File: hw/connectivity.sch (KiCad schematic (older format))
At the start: 130 parts, among them P1 CONN_13X3, P10 MICROSD, P11 CONN_9, P12 CONN_2, P13 CONN_6, P19 CONN_1, P2 CONN_4, P20 CONN_1, P21 CONN_1, P22 CONN_1, P3 CONN_4, P4 MICROUSB, P5 CONN_4, P6 CONN_6, P7 CONN_4, P8 CONN_4, P9 CONN_4, Q2 NTA4153NT1G, Q3 NTA4151PT1G, Q4 PDTC114EE, Q5 PDTC114EE, Q6 PDTC114EE, Q7 PDTC114EE, SW1 STG719, U1 XBEE, U11 SN74AHC1G86, U12 MAX4090, U2 LTC4411, U3 SN65HVD233, U4 ADP3338AKCZ-3.3, U5 LT1761-3.3, U6 EL1883

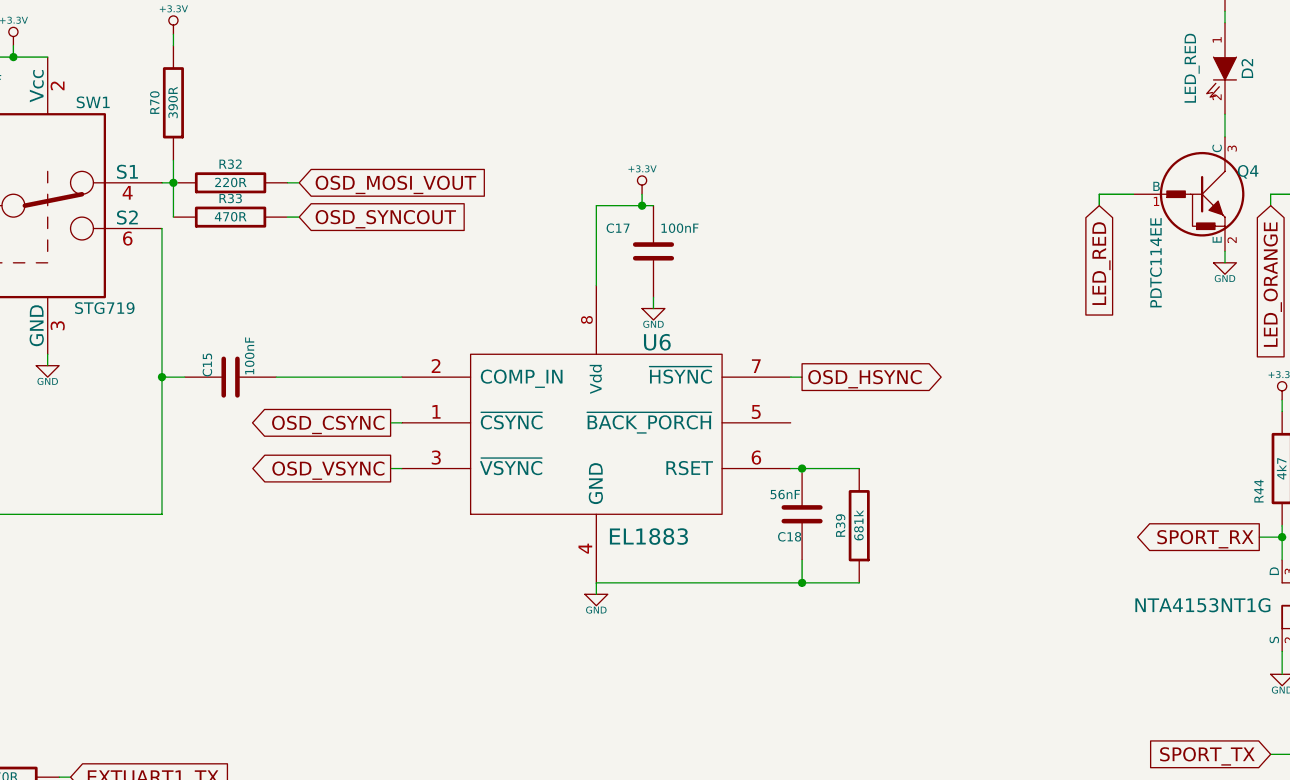
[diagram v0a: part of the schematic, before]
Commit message: hw: add chroma filter to sync separator, removed unused CSYNC signal
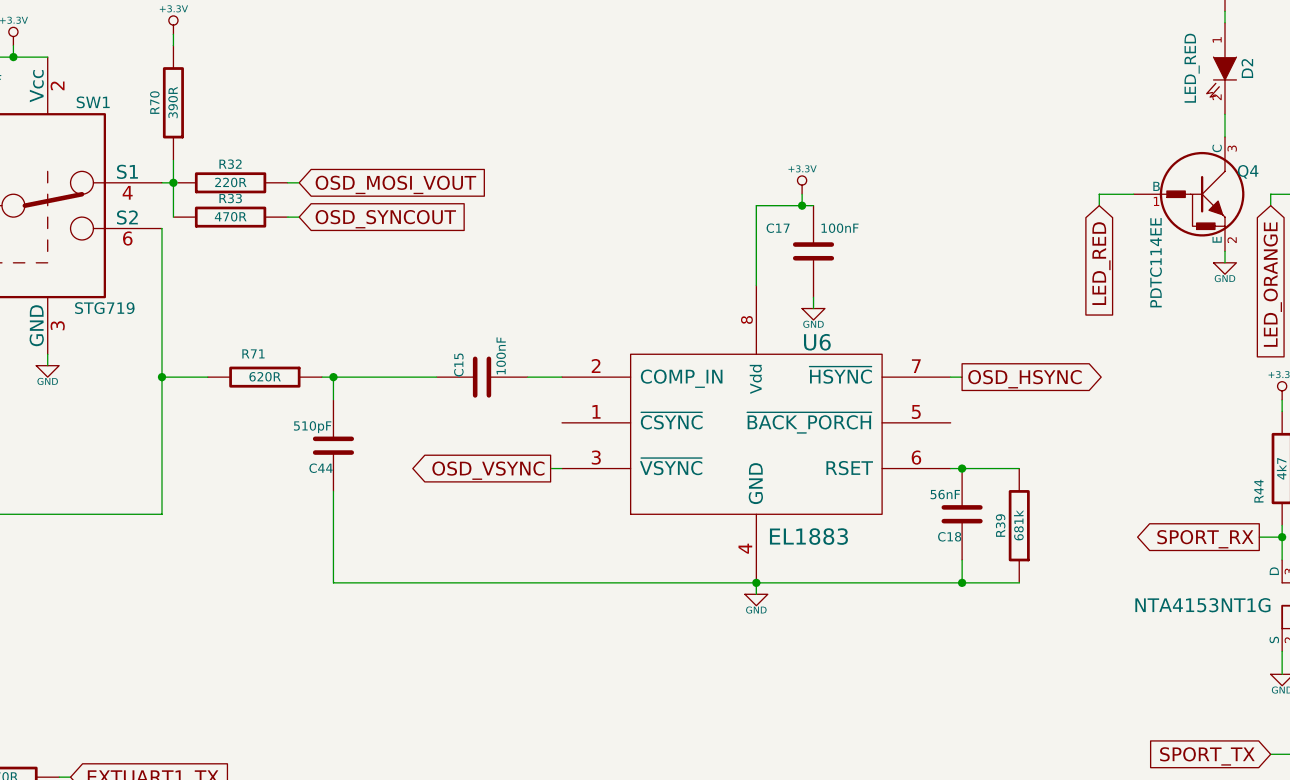
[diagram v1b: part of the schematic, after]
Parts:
- added C44: 510pF, c_0603, symbol C
- added R71: 620R, r_0603, symbol R
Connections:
- net labels removed: OSD_CSYNC
- wire segments 325 -> 327
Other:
- moved on the sheet: C15, C17, C18, R39, U6
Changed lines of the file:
@@
 L EL1883 U6
 U 1 1 52531AD1
-P 10800 5350
-F 0 "U6" H 11000 5750 70  0000 L CNN
-F 1 "EL1883" H 10850 4900 70  0000 L CNN
-F 2 "so-8" H 10800 5350 60  0001 C CNN
-F 3 "~" H 10800 5350 60  0000 C CNN
-	1    10800 5350
+P 11500 5350
+F 0 "U6" H 11700 5750 70  0000 L CNN
+F 1 "EL1883" H 11550 4900 70  0000 L CNN
+F 2 "so-8" H 11500 5350 60  0001 C CNN
+F 3 "~" H 11500 5350 60  0000 C CNN
+	1    11500 5350
 	1    0    0    -1
 $EndComp
@@
 L C C15
 U 1 1 525457CD
-P 9200 5100
-F 0 "C15" H 9200 5200 40  0000 L CNN
-F 1 "100nF" H 9206 5015 40  0000 L CNN
-F 2 "c_0603" H 9238 4950 30  0001 C CNN
-F 3 "~" H 9200 5100 60  0000 C CNN
-	1    9200 5100
-	0    -1   -1   0
-$EndComp
-Wire Wire Line
-	8900 5100 9000 5100
-Wire Wire Line
-	9400 5100 9950 5100
+P 10300 5100
+F 0 "C15" H 10300 5200 40  0000 L CNN
+F 1 "100nF" H 10306 5015 40  0000 L CNN
+F 2 "c_0603" H 10338 4950 30  0001 C CNN
+F 3 "~" H 10300 5100 60  0000 C CNN
+	1    10300 5100
+	0    -1   -1   0
+$EndComp
+Wire Wire Line
+	8900 5100 9100 5100
 $Comp
 L C C18
 U 1 1 52545C9B
-P 11700 5700
-F 0 "C18" H 11700 5800 40  0000 L CNN
-F 1 "56nF" H 11706 5615 40  0000 L CNN
-F 2 "c_0603" H 11738 5550 30  0001 C CNN
-F 3 "~" H 11700 5700 60  0000 C CNN
-	1    11700 5700
+P 12400 5700
+F 0 "C18" H 12400 5800 40  0000 L CNN
+F 1 "56nF" H 12406 5615 40  0000 L CNN
+F 2 "c_0603" H 12438 5550 30  0001 C CNN
+F 3 "~" H 12400 5700 60  0000 C CNN
+	1    12400 5700
 	-1   0    0    1
 $EndComp
@@
 L R R39
 U 1 1 52545CAD
-P 11950 5750
-F 0 "R39" V 12030 5750 40  0000 C CNN
-F 1 "681k" V 11950 5750 40  0000 C CNN
-F 2 "r_0603" V 11880 5750 30  0001 C CNN
-F 3 "~" H 11950 5750 30  0000 C CNN
-	1    11950 5750
+P 12650 5750
+F 0 "R39" V 12730 5750 40  0000 C CNN
+F 1 "681k" V 12650 5750 40  0000 C CNN
+F 2 "r_0603" V 12580 5750 30  0001 C CNN
+F 3 "~" H 12650 5750 30  0000 C CNN
+	1    12650 5750
 	-1   0    0    1
 $EndComp
 Wire Wire Line
-	11650 5500 11950 5500
-Connection ~ 11700 5500
-Wire Wire Line
-	10800 6000 11950 6000
-Wire Wire Line
-	11700 6000 11700 5900
-Connection ~ 11700 6000
+	12350 5500 12650 5500
+Connection ~ 12400 5500
+Wire Wire Line
+	9650 6000 12650 6000
+Wire Wire Line
+	12400 6000 12400 5900
+Connection ~ 12400 6000
 $Comp
 L C C17
 U 1 1 525463CB
-P 11050 4550
-F 0 "C17" H 11150 4450 40  0000 L CNN
-F 1 "100nF" H 10850 4450 40  0000 L CNN
-F 2 "c_0603" H 11088 4400 30  0001 C CNN
-F 3 "~" H 11050 4550 60  0000 C CNN
-	1    11050 4550
+P 11750 4550
+F 0 "C17" H 11850 4450 40  0000 L CNN
+F 1 "100nF" H 11550 4450 40  0000 L CNN
+F 2 "c_0603" H 11788 4400 30  0001 C CNN
+F 3 "~" H 11750 4550 60  0000 C CNN
+	1    11750 4550
 	-1   0    0    1
 $EndComp
 Wire Wire Line
-	10800 4700 10800 4350
-Wire Wire Line
-	10800 4350 11050 4350
+	11500 4700 11500 4350
+Wire Wire Line
+	11500 4350 11750 4350
 $Comp
 L GND #PWR049
 U 1 1 525464F6
-P 11050 4800
-F 0 "#PWR049" H 11050 4800 30  0001 C CNN
-F 1 "GND" H 11050 4730 30  0000 C CNN
-F 2 "" H 11050 4800 60  0000 C CNN
-F 3 "" H 11050 4800 60  0000 C CNN
-	1    11050 4800
-	1    0    0    -1
-$EndComp
-Wire Wire Line
-	11050 4750 11050 4800
+P 11750 4800
+F 0 "#PWR049" H 11750 4800 30  0001 C CNN
+F 1 "GND" H 11750 4730 30  0000 C CNN
+F 2 "" H 11750 4800 60  0000 C CNN
+F 3 "" H 11750 4800 60  0000 C CNN
+	1    11750 4800
+	1    0    0    -1
+$EndComp
+Wire Wire Line
+	11750 4750 11750 4800
 $Comp
 L GND #PWR050
 U 1 1 52546623
-P 10800 6050
-F 0 "#PWR050" H 10800 6050 30  0001 C CNN
-F 1 "GND" H 10800 5980 30  0000 C CNN
-F 2 "" H 10800 6050 60  0000 C CNN
-F 3 "" H 10800 6050 60  0000 C CNN
-	1    10800 6050
-	1    0    0    -1
-$EndComp
-Wire Wire Line
-	10800 6000 10800 6050
-Text GLabel 11700 5100 2    60   Output ~ 0
+P 11500 6050
+F 0 "#PWR050" H 11500 6050 30  0001 C CNN
+F 1 "GND" H 11500 5980 30  0000 C CNN
+F 2 "" H 11500 6050 60  0000 C CNN
+F 3 "" H 11500 6050 60  0000 C CNN
+	1    11500 6050
+	1    0    0    -1
+$EndComp
+Wire Wire Line
+	11500 6000 11500 6050
+Text GLabel 12400 5100 2    60   Output ~ 0
 OSD_HSYNC
 Wire Wire Line
-	11650 5100 11700 5100
-Text GLabel 9900 5300 0    60   Output ~ 0
-OSD_CSYNC
-Text GLabel 9900 5500 0    60   Output ~ 0
+	12350 5100 12400 5100
+Text GLabel 10600 5500 0    60   Output ~ 0
 OSD_VSYNC
 Wire Wire Line
-	9900 5500 9950 5500
+	10600 5500 10650 5500
 Text Notes 4900 5200 0    60   ~ 0
 OSD
@@
 L +3.3V #PWR053
 U 1 1 525B33A8
-P 11000 4300
-F 0 "#PWR053" H 11000 4260 30  0001 C CNN
-F 1 "+3.3V" H 11000 4410 30  0000 C CNN
-F 2 "" H 11000 4300 60  0000 C CNN
-F 3 "" H 11000 4300 60  0000 C CNN
-	1    11000 4300
-	1    0    0    -1
-$EndComp
-Wire Wire Line
-	11000 4300 11000 4350
-Connection ~ 11000 4350
-Wire Wire Line
-	9900 5300 9950 5300
+P 11700 4300
+F 0 "#PWR053" H 11700 4260 30  0001 C CNN
+F 1 "+3.3V" H 11700 4410 30  0000 C CNN
+F 2 "" H 11700 4300 60  0000 C CNN
+F 3 "" H 11700 4300 60  0000 C CNN
+	1    11700 4300
+	1    0    0    -1
+$EndComp
+Wire Wire Line
+	11700 4300 11700 4350
+Connection ~ 11700 4350
 Wire Wire Line
 	1450 700  1900 700
@@
 	1500 5450 1500 5600
 Connection ~ 1500 5600
+Wire Wire Line
+	10500 5100 10650 5100
+$Comp
+L R R71
+U 1 1 5424340E
+P 9350 5100
+F 0 "R71" V 9250 5050 40  0000 C CNN
+F 1 "620R" V 9350 5100 40  0000 C CNN
+F 2 "r_0603" V 9280 5100 30  0001 C CNN
+F 3 "~" H 9350 5100 30  0000 C CNN
+	1    9350 5100
+	0    1    1    0
+$EndComp
+$Comp
+L C C44
+U 1 1 542435BE
+P 9650 5400
+F 0 "C44" H 9650 5500 40  0000 L CNN
+F 1 "510pF" H 9656 5315 40  0000 L CNN
+F 2 "c_0603" H 9688 5250 30  0001 C CNN
+F 3 "~" H 9650 5400 60  0000 C CNN
+	1    9650 5400
+	-1   0    0    1
+$EndComp
+Wire Wire Line
+	9600 5100 10100 5100
+Wire Wire Line
+	9650 5100 9650 5200
+Connection ~ 9650 5100
+Wire Wire Line
+	9650 5600 9650 6000
+Connection ~ 11500 6000
 $EndSCHEMATC

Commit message: hw: USB Vbus resistor value lowered to 18k
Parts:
- R18: value 39k -> 18k
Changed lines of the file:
@@
 Sheet 2 3
 Title "DRACO - connectivity sheet"
-Date "25 sep 2014"
+Date "19 nov 2014"
 Rev "1.1"
 Comp "dandys"
@@
 P 1750 5450
 F 0 "R18" V 1850 5550 40  0000 C CNN
-F 1 "39k" V 1750 5450 40  0000 C CNN
+F 1 "18k" V 1750 5450 40  0000 C CNN
 F 2 "r_0603" V 1680 5450 30  0001 C CNN
 F 3 "~" H 1750 5450 30  0000 C CNN
